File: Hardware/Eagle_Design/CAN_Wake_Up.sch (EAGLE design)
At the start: 32 parts, among them IC1 STM32F10XCXT6, IC4 LM1117MP-5.0, IC5 LM1117MP-3.3, Q1 8MHz

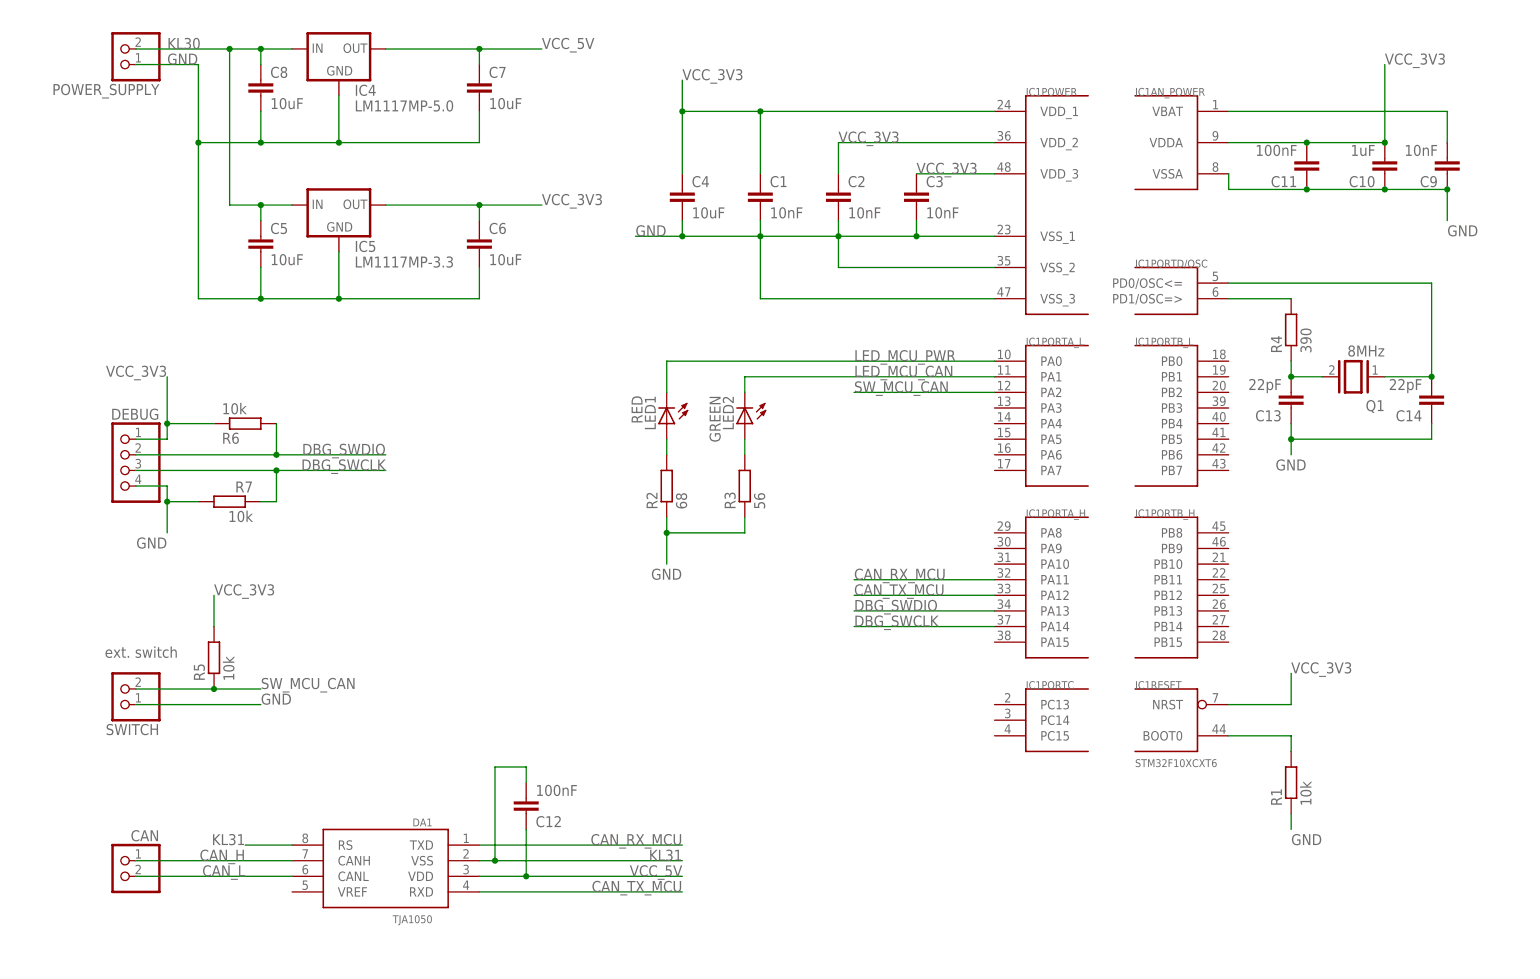
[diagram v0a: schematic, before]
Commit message: Renamed schematic and layout directory. Updated Schematic, replaced crystal with SMD variant. Added initial board layout file.
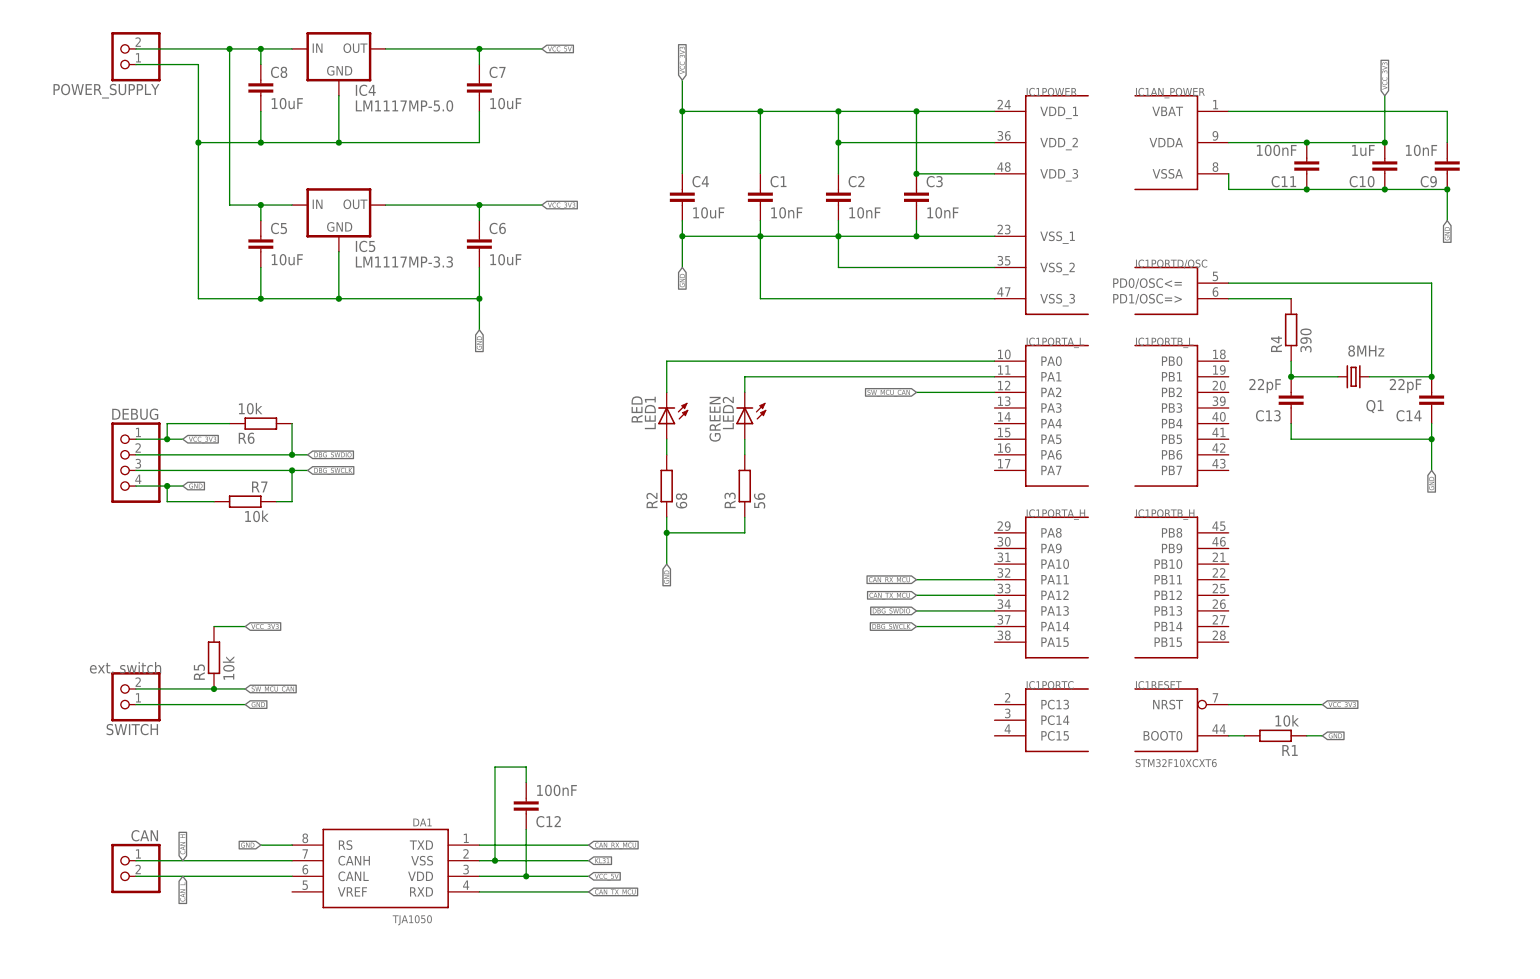
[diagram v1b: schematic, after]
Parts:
- Q1: device special:XTAL -> crystal:CRYSTALHC49UP
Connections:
- net GND: now also DA1.RS
- net KL31: no longer DA1.RS
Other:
- moved on the sheet: R1, R6, R7

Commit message: Started on PCB layout.
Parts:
- removed DEBUG: (no value), pinhead:PINHD-1X4
- added DBG_GND, DBG_SWCLK, DBG_SWDIO, DBG_VCC_3V3: TPB1,27, testpad:TPB1,27
- LED1, LED2: device led:LED3MM -> led:LEDSML0805
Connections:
- net DBG_SWCLK: now also DBG_SWCLK.TP; no longer DEBUG.3
- net DBG_SWDIO: now also DBG_SWDIO.TP; no longer DEBUG.2
- net GND: now also DBG_GND.TP; no longer DEBUG.4
- net VCC_3V3: now also DBG_VCC_3V3.TP; no longer DEBUG.1
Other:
- moved on the sheet: R6, R7

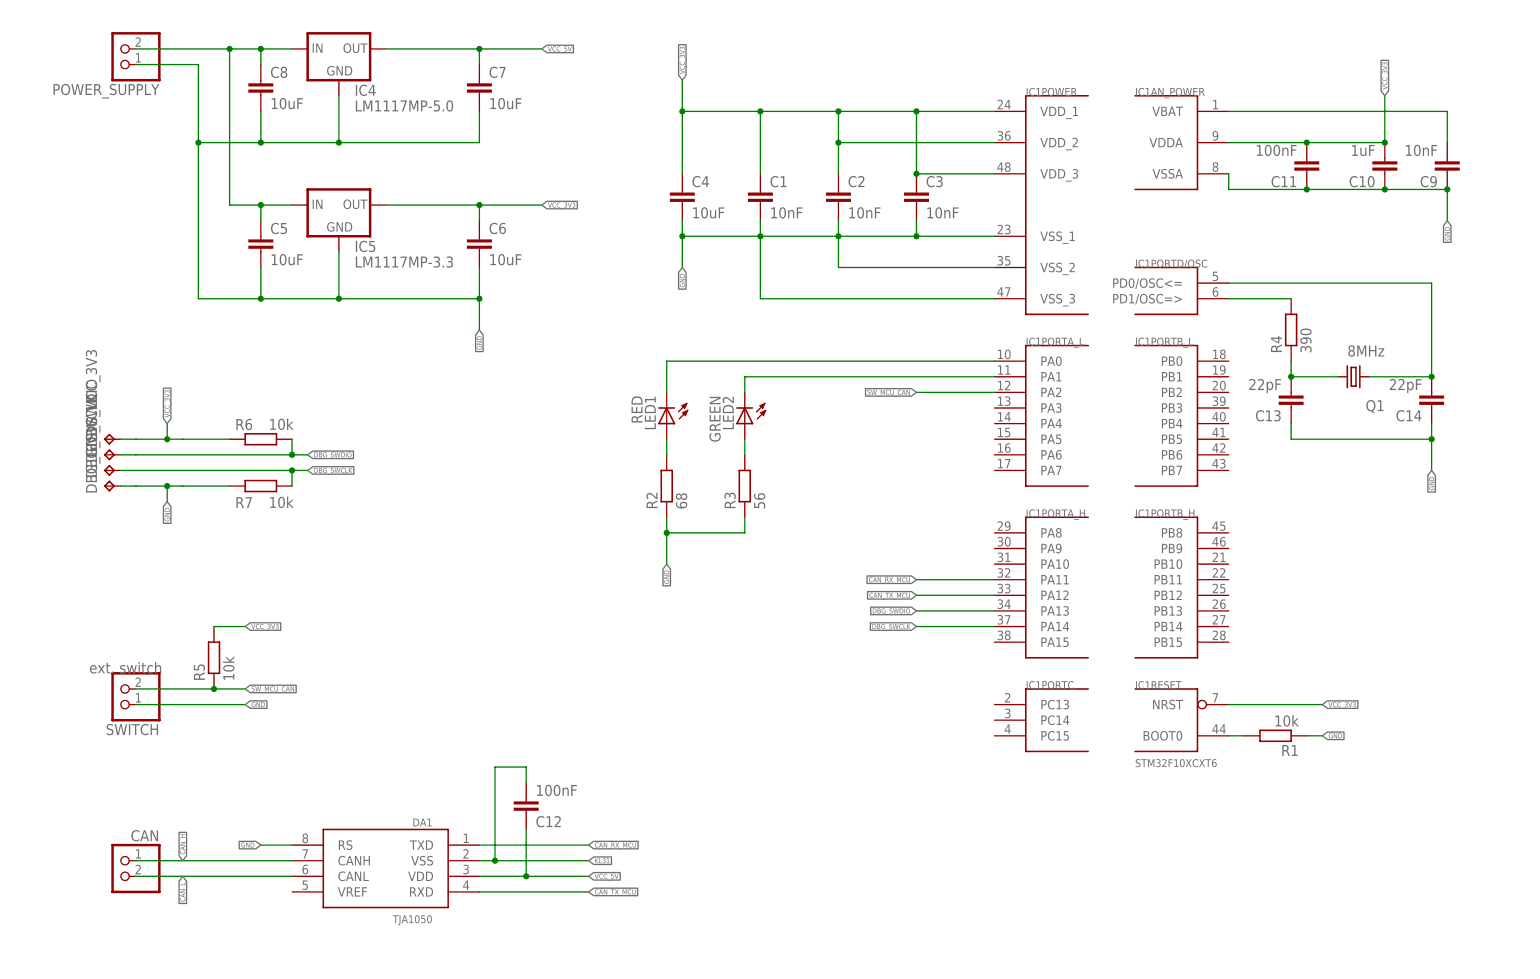
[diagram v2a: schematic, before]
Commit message: Continued on layout. Not yet fully routable. PCB need to be resized.
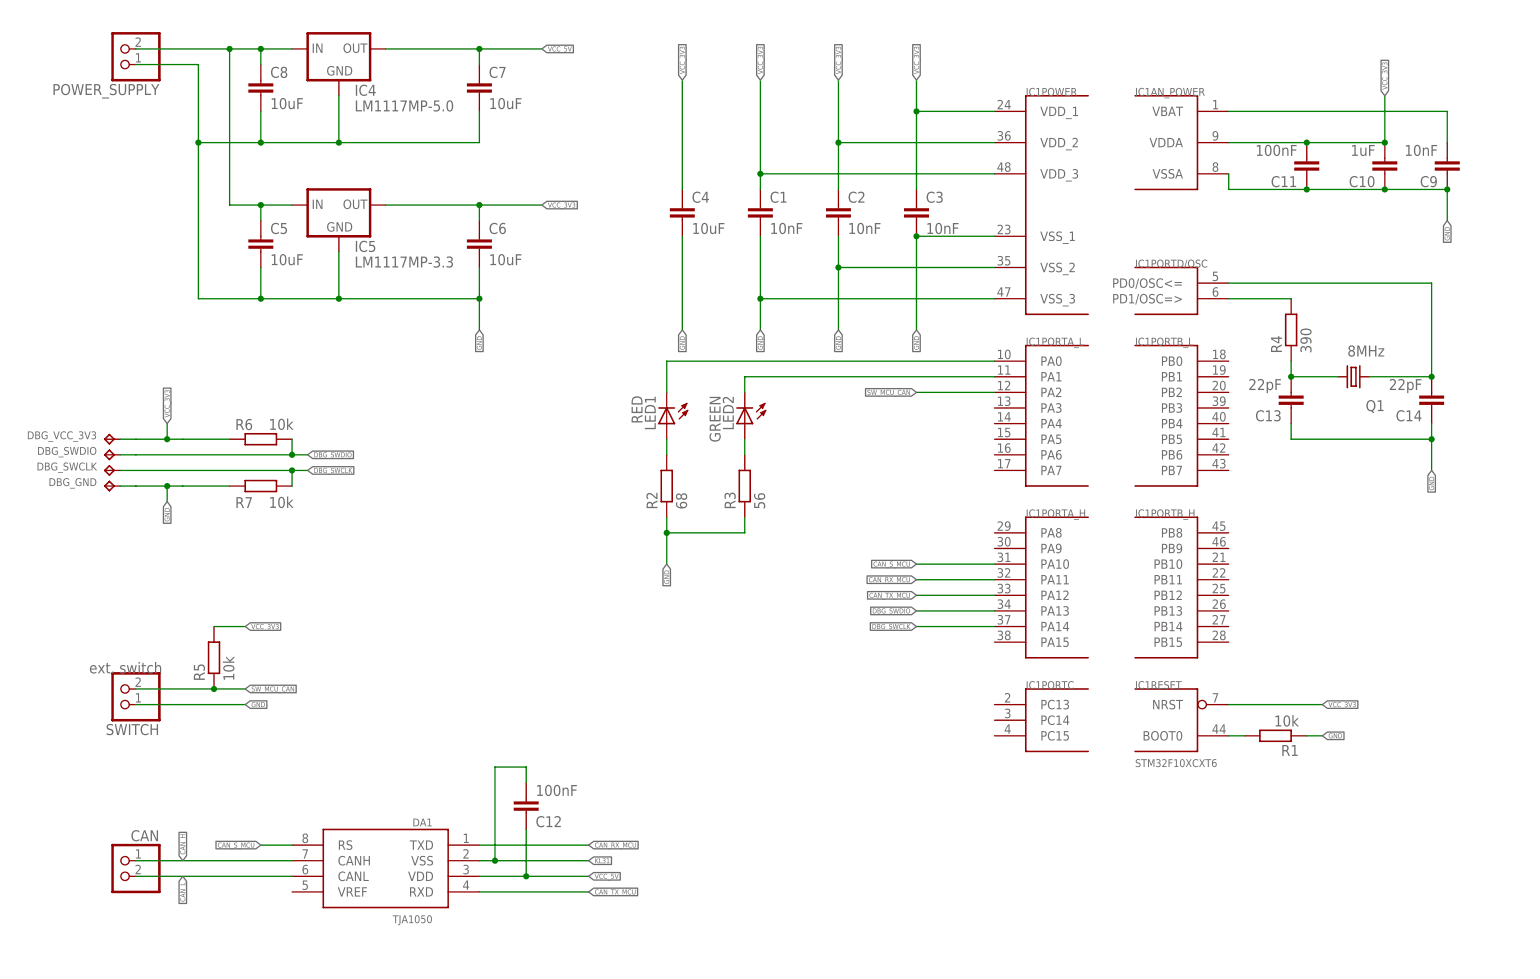
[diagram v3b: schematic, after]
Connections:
- new net CAN_S_MCU: DA1.RS, IC1PORTA_H.PA10
- net GND: no longer DA1.RS
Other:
- moved on the sheet: C1, C2, C3, C4

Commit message: Finished board layout. First order at seeedstudio.com
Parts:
- removed CAN, POWER_SUPPLY, SWITCH: (no value), pinhead:PINHD-1X2
- added DSUB-9: CAN, con-subd:F09HPS
- added GND, KL30: (no value), pinhead:PINHD-1X1
- added H1, H2, H3, H4: SPECIAL_DRILL_0.1000, special-drill:SPECIAL_DRILL_0.1000
- added R8: 10k, rcl:R-EU_R0805
- added S1: 9077-1, switch-misc:9077-1
- renumbered LED1 to LED_PWR, LED2 to LED_TX
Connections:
- removed net KL31: C12.2, DA1.VSS
- new net N$8: IC1PORTB_L.PB2, R8.1
- net CAN_H: now also DSUB-9-7.F; no longer CAN.1
- net CAN_L: now also DSUB-9-2.F; no longer CAN.2
- net GND: now also C12.2, DA1.VSS, DSUB-9-3.F, DSUB-9-G.G1, GND.1, H1.1, H2.1, H3.1, H4.1, R8.2, S1.S; no longer POWER_SUPPLY.1, SWITCH.1
- net KL30: now also KL30.1; no longer POWER_SUPPLY.2
- net SW_MCU_CAN: now also S1.P; no longer SWITCH.2
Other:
- moved on the sheet: C13, C14, Q1, R4, R5

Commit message: New version. Added Eagle BOM (.csv) file.
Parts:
- DSUB-9: device con-subd:F09HPS -> con-subd:M09HPS
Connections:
- net CAN_H: now also DSUB-9-7.M; no longer DSUB-9-7.F
- net CAN_L: now also DSUB-9-2.M; no longer DSUB-9-2.F
- net GND: now also DSUB-9-3.M; no longer DSUB-9-3.F
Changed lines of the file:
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@@
 <part name="DBG_SWCLK" library="testpad" library_urn="urn:adsk.eagle:library:385" deviceset="TP" device="B1,27" package3d_urn="urn:adsk.eagle:package:27944/1" value="TPB1,27"/>
 <part name="DBG_GND" library="testpad" library_urn="urn:adsk.eagle:library:385" deviceset="TP" device="B1,27" package3d_urn="urn:adsk.eagle:package:27944/1" value="TPB1,27"/>
-<part name="DSUB-9" library="con-subd" library_urn="urn:adsk.eagle:library:189" deviceset="F09HPS" device="" package3d_urn="urn:adsk.eagle:package:10232/1" value="CAN"/>
+<part name="DSUB-9" library="con-subd" library_urn="urn:adsk.eagle:library:189" deviceset="M09HPS" device="" package3d_urn="urn:adsk.eagle:package:10236/1" value="CAN"/>
 <part name="KL30" library="pinhead" library_urn="urn:adsk.eagle:library:325" deviceset="PINHD-1X1" device="" package3d_urn="urn:adsk.eagle:package:22485/2"/>
 <part name="GND" library="pinhead" library_urn="urn:adsk.eagle:library:325" deviceset="PINHD-1X1" device="" package3d_urn="urn:adsk.eagle:package:22485/2"/>
@@
 <wire x1="-68.58" y1="-5.08" x2="-81.28" y2="-5.08" width="0.1524" layer="91"/>
 <wire x1="-81.28" y1="-5.08" x2="-86.36" y2="-5.08" width="0.1524" layer="91"/>
-<pinref part="DSUB-9" gate="-2" pin="F"/>
+<pinref part="DSUB-9" gate="-2" pin="M"/>
 <wire x1="-86.36" y1="-10.16" x2="-93.98" y2="-10.16" width="0.1524" layer="91"/>
 <wire x1="-86.36" y1="-5.08" x2="-86.36" y2="-10.16" width="0.1524" layer="91"/>
@@
 </segment>
 <segment>
-<pinref part="DSUB-9" gate="-3" pin="F"/>
+<pinref part="DSUB-9" gate="-3" pin="M"/>
 <wire x1="-93.98" y1="-7.62" x2="-88.9" y2="-7.62" width="0.1524" layer="91"/>
 <wire x1="-88.9" y1="-7.62" x2="-88.9" y2="-15.24" width="0.1524" layer="91"/>
@@
 <pinref part="DA1" gate="G$1" pin="CANH"/>
 <wire x1="-68.58" y1="-2.54" x2="-86.36" y2="-2.54" width="0.1524" layer="91"/>
-<pinref part="DSUB-9" gate="-7" pin="F"/>
+<pinref part="DSUB-9" gate="-7" pin="M"/>
 <wire x1="-93.98" y1="2.54" x2="-86.36" y2="2.54" width="0.1524" layer="91"/>
 <label x="-81.28" y="-2.54" size="0.8128" layer="95" rot="R90" xref="yes"/>

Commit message: Fixed ignores again
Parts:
- removed DBG_GND, DBG_SWCLK, DBG_SWDIO, DBG_VCC_3V3: TPB1,27, testpad:TPB1,27
- removed GND, KL30: (no value), pinhead:PINHD-1X1
- added C15: 100nF, rcl:C-EUC0805
- added DEBUG: (no value), pinhead:PINHD-1X4
- added POWER, SERIAL: (no value), pinhead:PINHD-1X2
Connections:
- new net N$9: C15.1, IC1RESET.NRST
- new net USART1_TX: IC1PORTA_H.PA9, SERIAL.1
- new net USART_1_RX: IC1PORTA_H.PA10, SERIAL.2
- net CAN_RX_MCU: now also DA1.RXD; no longer DA1.TXD
- net CAN_S_MCU: now also IC1PORTA_H.PA15; no longer IC1PORTA_H.PA10
- net CAN_TX_MCU: now also DA1.TXD; no longer DA1.RXD
- net DBG_SWCLK: now also DEBUG.3; no longer DBG_SWCLK.TP
- net DBG_SWDIO: now also DEBUG.2; no longer DBG_SWDIO.TP
- net GND: now also C15.2, POWER.2; no longer DBG_GND.TP, GND.1
- net KL30: now also POWER.1; no longer KL30.1
- net VCC_3V3: no longer DBG_VCC_3V3.TP, IC1RESET.NRST
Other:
- moved on the sheet: LED_PWR, LED_TX, R1, R2, R3, R6, R7

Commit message: Latest hardware revision: rev2
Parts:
- DEBUG: device pinhead:PINHD-1X4 -> pinhead:PINHD-1X5
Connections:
- net GND: now also DEBUG.4
- net N$9: now also DEBUG.5
- net VCC_3V3: now also DEBUG.1
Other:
- moved on the sheet: H1, H2, H3, H4, POWER, R6, R7
